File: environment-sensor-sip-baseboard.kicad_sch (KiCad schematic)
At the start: 58 parts, among them J1 USB-C_GCT_USB4105-GF-A, J2 JST_SH_1x4_SM04B-SRSS-TB-LF-SN, J3 JST_SH_1x4_SM04B-SRSS-TB-LF-SN, U1 Antmicro_GEM3, U5 SHT45, U6 BME280

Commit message: [#61553] Route PCB
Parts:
- added TP21, TP22: TP_1.5mm_SMD, antmicro-footprints:TP_SMD_1.5mm, symbol antmicroTestPoints:TP_1.5mm_SMD
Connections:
- net +3V3: now also D7.1 (C), D9.1 (C); no longer D7.2 (A), D9.2 (A)
- net GND: now also D1.2 (A), D2.2 (A), D3.2 (A), D4.2 (A), D7.2 (A), D9.2 (A), U1.A1, U1.A2, U1.A3, U1.A4, U1.A5, U1.A6, U1.B1, U1.C1, TP21.1, TP22.1; no longer D1.1 (C), D2.1 (C), D3.1 (C), D4.1 (C), D7.1 (C), D9.1 (C)
- net LD2: now also LD2.2 (A); no longer LD2.1 (C)
- net USB_CC1: now also D3.1 (C); no longer D3.2 (A)
- net USB_CC2: now also D4.1 (C); no longer D4.2 (A)
- net VBUS: now also D1.1 (C), D2.1 (C), LD1.2 (A); no longer D1.2 (A), D2.2 (A), LD1.1 (C)
- net at R5.2: now also LD2.1 (C); no longer LD2.2 (A)
- net at R12.2: now also LD1.1 (C); no longer LD1.2 (A)
- no-connect marks 22 -> 14
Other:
- moved on the sheet: D1, D2, D3, D4, D7, D9, LD1, LD2

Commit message: [#61553] Improve schematic readability
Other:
- note added: "Mechanical"
- note added: "Misc"
- note added: "SiP"
- note added: "Test Points"
- title: Environmental Sensor -> SiP Baseboard
- moved on the sheet: BAT1, C13, C2, C25, C26, C27, C28, C4, D1, D2, D3, D4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

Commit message: [#61553] Update title block
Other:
- company: Antmicro Ltd -> Antmicro 
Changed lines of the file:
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@@
     (date "2024-06-28")
     (rev "1.0.0")
-    (company "Antmicro Ltd")
+    (company "Antmicro ")
     (comment 1 "www.antmicro.com")
   )

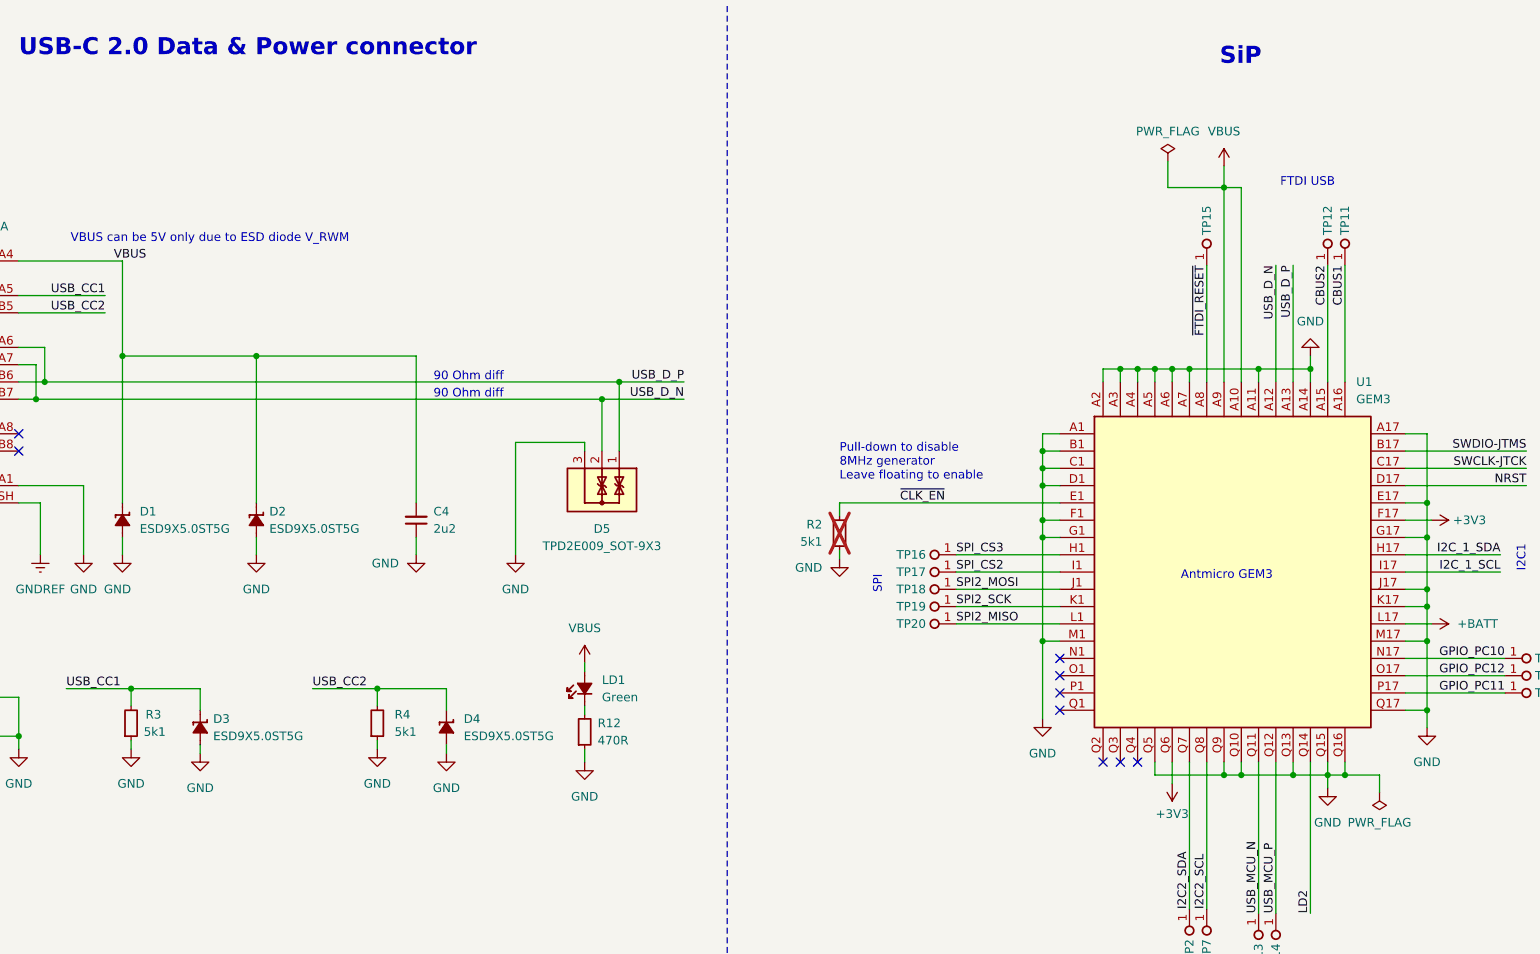
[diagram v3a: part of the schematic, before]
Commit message: [#61553] Fix ERC
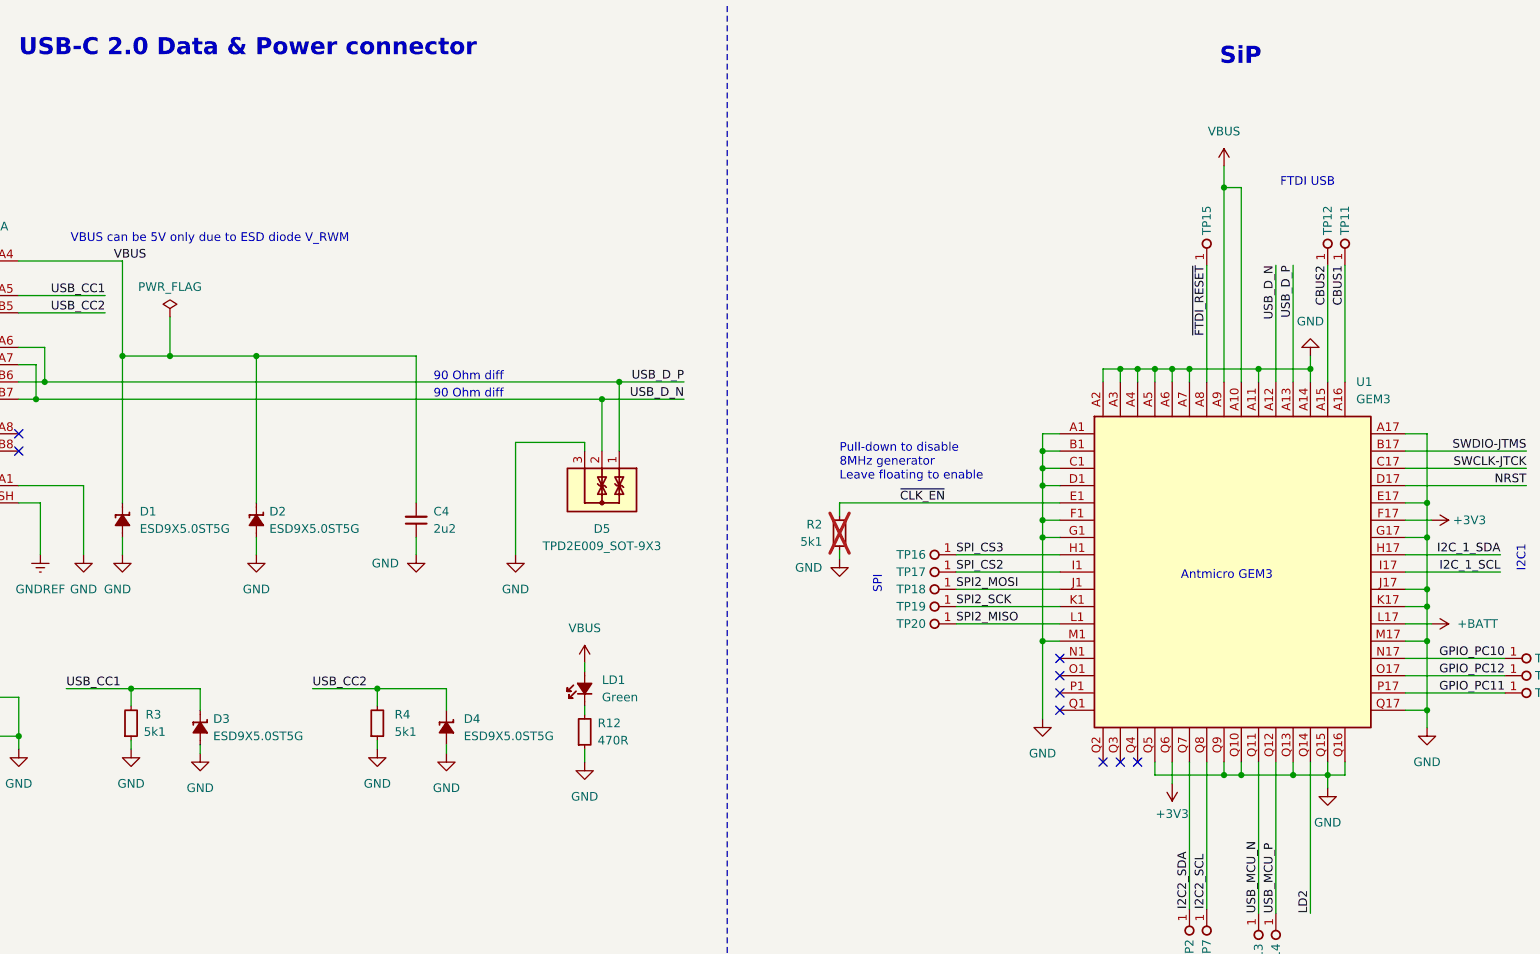
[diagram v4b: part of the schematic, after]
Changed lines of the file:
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@@
   (junction (at 49.53 67.945) (diameter 0) (color 0 0 0 0)
   )
-  (junction (at 240.665 125.73) (diameter 0) (color 0 0 0 0)
-  )
   (junction (at 238.125 125.73) (diameter 0) (color 0 0 0 0)
   )
@@
   )
   (junction (at 252.73 116.205) (diameter 0) (color 0 0 0 0)
+  )
+  (junction (at 67.945 64.135) (diameter 0) (color 0 0 0 0)
   )
   (junction (at 131.445 70.485) (diameter 0) (color 0 0 0 0)
@@
     (stroke (width 0) (type default))
   )
-  (wire (pts (xy 214.63 39.37) (xy 214.63 35.56))
+  (wire (pts (xy 67.945 58.42) (xy 67.945 64.135))
     (stroke (width 0) (type default))
   )
@@
   )
   (wire (pts (xy 205.105 66.04) (xy 205.105 67.945))
+    (stroke (width 0) (type default))
+  )
+  (wire (pts (xy 67.945 64.135) (xy 80.645 64.135))
     (stroke (width 0) (type default))
   )
@@
     (stroke (width 0) (type default))
   )
-  (wire (pts (xy 222.885 39.37) (xy 214.63 39.37))
-    (stroke (width 0) (type default))
-  )
-  (wire (pts (xy 240.665 125.73) (xy 245.745 125.73))
-    (stroke (width 0) (type default))
-  )
   (wire (pts (xy 49.53 67.945) (xy 133.985 67.945))
     (stroke (width 0) (type default))
@@
     (stroke (width 0) (type default))
   )
-  (wire (pts (xy 245.745 125.73) (xy 245.745 128.27))
-    (stroke (width 0) (type default))
-  )
   (wire (pts (xy 198.12 219.075) (xy 198.12 211.455))
     (stroke (width 0) (type default))
@@
     (stroke (width 0) (type default))
   )
-  (wire (pts (xy 60.96 64.135) (xy 80.645 64.135))
+  (wire (pts (xy 60.96 64.135) (xy 67.945 64.135))
     (stroke (width 0) (type default))
   )
@@
     )
   )
-  (symbol (lib_id "antmicropower:PWR_FLAG") (at 214.63 35.56 0) (unit 1)
-    (in_bom yes) (on_board yes) (dnp no) (fields_autoplaced)
-    (property "Reference" "#FLG01" (at 214.63 33.655 0)
-      (effects (font (size 1.27 1.27)) hide)
-    )
-    (property "Value" "PWR_FLAG" (at 214.63 31.115 0)
+  (symbol (lib_id "antmicropower:PWR_FLAG") (at 67.945 58.42 0) (unit 1)
+    (in_bom yes) (on_board yes) (dnp no) (fields_autoplaced)
+    (property "Reference" "#FLG01" (at 67.945 56.515 0)
+      (effects (font (size 1.27 1.27)) hide)
+    )
+    (property "Value" "PWR_FLAG" (at 67.945 53.975 0)
       (effects (font (size 1.27 1.27)))
     )
-    (property "Footprint" "" (at 214.63 35.56 0)
-      (effects (font (size 1.27 1.27)) hide)
-    )
-    (property "Datasheet" "" (at 214.63 35.56 0)
+    (property "Footprint" "" (at 67.945 58.42 0)
+      (effects (font (size 1.27 1.27)) hide)
+    )
+    (property "Datasheet" "" (at 67.945 58.42 0)
       (effects (font (size 1.27 1.27)) hide)
     )
@@
         )
       )
-    )
-  )
-  (symbol (lib_id "antmicropower:PWR_FLAG") (at 245.745 128.27 180) (unit 1)
-    (in_bom yes) (on_board yes) (dnp no) (fields_autoplaced)
-    (property "Reference" "#FLG02" (at 245.745 130.175 0)
-      (effects (font (size 1.27 1.27)) hide)
-    )
-    (property "Value" "PWR_FLAG" (at 245.745 132.715 0)
-      (effects (font (size 1.27 1.27)))
-    )
-    (property "Footprint" "" (at 245.745 128.27 0)
-      (effects (font (size 1.27 1.27)) hide)
-    )
-    (property "Datasheet" "" (at 245.745 128.27 0)
-      (effects (font (size 1.27 1.27)) hide)
-    )
-    (pin "1")
-    (instances
-      (project "environment-sensor-sip-baseboard"
-        (path "/8eef0f5e-ea92-4309-8bfa-5d89a1db9ae8"
-          (reference "#FLG02") (unit 1)
-        )
-      )

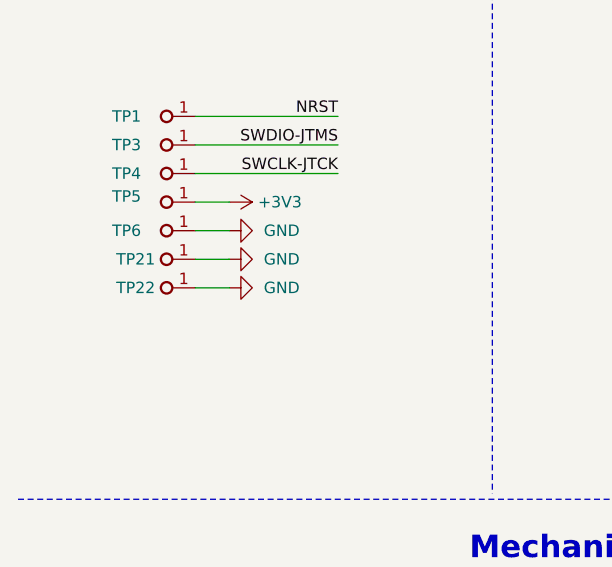
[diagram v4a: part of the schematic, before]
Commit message: [#61553] Fix logo at PCB
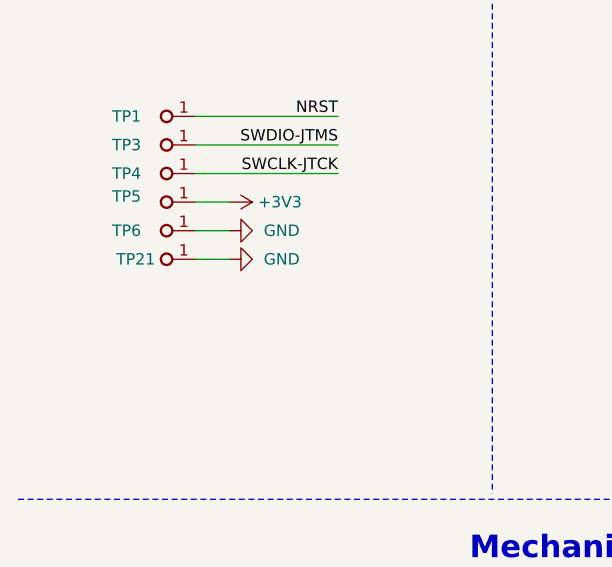
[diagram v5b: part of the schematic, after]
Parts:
- removed TP22: TP_1.5mm_SMD, antmicro-footprints:TP_SMD_1.5mm, symbol antmicroTestPoints:TP_1.5mm_SMD
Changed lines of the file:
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@@
     (stroke (width 0) (type dash))
-  )
-  (wire (pts (xy 36.83 234.315) (xy 33.02 234.315))
-    (stroke (width 0) (type default))
   )
   (wire (pts (xy 218.44 226.695) (xy 218.44 227.965))
@@
         (path "/8eef0f5e-ea92-4309-8bfa-5d89a1db9ae8"
           (reference "#PWR072") (unit 1)
-        )
-      )
-    )
-  )
-  (symbol (lib_id "antmicroTestPoints:TP_1.5mm_SMD") (at 33.02 234.315 180) (unit 1)
-    (in_bom yes) (on_board yes) (dnp no)
-    (property "Reference" "TP22" (at 28.575 234.315 0)
-      (effects (font (size 1.27 1.27) (thickness 0.15)) (justify left))
-    )
-    (property "Value" "TP_1.5mm_SMD" (at 17.78 226.695 0)
-      (effects (font (size 1.27 1.27) (thickness 0.15)) (justify left bottom) hide)
-    )
-    (property "Footprint" "antmicro-footprints:TP_SMD_1.5mm" (at 17.78 224.155 0)
-      (effects (font (size 1.27 1.27) (thickness 0.15)) (justify left bottom) hide)
-    )
-    (property "Datasheet" "" (at 17.78 221.615 0)
-      (effects (font (size 1.27 1.27) (thickness 0.15)) (justify left bottom) hide)
-    )
-    (property "MPN" "" (at 33.02 234.315 0)
-      (effects (font (size 1.27 1.27)) hide)
-    )
-    (property "Manufacturer" "" (at 33.02 234.315 0)
-      (effects (font (size 1.27 1.27)) hide)
-    )
-    (property "Author" "Antmicro" (at 17.78 219.075 0)
-      (effects (font (size 1.27 1.27) (thickness 0.15)) (justify left bottom) hide)
-    )
-    (property "License" "Apache-2.0" (at 17.78 216.535 0)
-      (effects (font (size 1.27 1.27) (thickness 0.15)) (justify left bottom) hide)
-    )
-    (property "Public" "False" (at 17.78 213.995 0)
-      (effects (font (size 1.27 1.27)) (justify left bottom) hide)
-    )
-    (pin "1")
-    (instances
-      (project "environment-sensor-sip-baseboard"
-        (path "/8eef0f5e-ea92-4309-8bfa-5d89a1db9ae8"
-          (reference "TP22") (unit 1)
         )
       )
@@
         )
       )
-    )
-  )
-  (symbol (lib_id "antmicropower:GND") (at 36.83 234.315 90) (mirror x) (unit 1)
-    (in_bom yes) (on_board yes) (dnp no) (fields_autoplaced)
-    (property "Reference" "#PWR028" (at 43.18 234.315 0)
-      (effects (font (size 1.27 1.27)) hide)
-    )
-    (property "Value" "GND" (at 40.64 234.315 90)
-      (effects (font (size 1.27 1.27)) (justify right))
-    )
-    (property "Footprint" "" (at 36.83 234.315 0)
-      (effects (font (size 1.27 1.27)) hide)
-    )
-    (property "Datasheet" "" (at 36.83 234.315 0)
-      (effects (font (size 1.27 1.27)) hide)
-    )
-    (property "Author" "Antmicro" (at 44.45 243.205 0)
-      (effects (font (size 1.27 1.27) (thickness 0.15)) (justify left bottom) hide)
-    )
-    (property "License" "Apache-2.0" (at 46.99 243.205 0)
-      (effects (font (size 1.27 1.27) (thickness 0.15)) (justify left bottom) hide)
-    )
-    (pin "1")
-    (instances
-      (project "environment-sensor-sip-baseboard"
-        (path "/8eef0f5e-ea92-4309-8bfa-5d89a1db9ae8"
-          (reference "#PWR028") (unit 1)
-        )
-      )

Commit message: [#62396] Update components
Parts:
- U1: value Antmicro_GEM3 -> Myra-231F1F08; footprint antmicro-footprints:LGA-64_11.4x11.4mm_GEM3-footprint -> antmicro-footprints:LGA-64_11.4x11.4mm_Myra; symbol antmicroModules:GEM3 -> antmicroModules:Myra-231F1F08; MPN GEM3 -> Myra-231F1F08
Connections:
- net GND: no longer U1.B1, U1.C1
- no-connect marks 14 -> 7
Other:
- note removed: "Antmicro GEM3"
- note removed: "FTDI USB"
- note removed: "I2C1"
- note removed: "I2C2"
- note removed: "SPI"
- note removed: "STM USB"
- moved on the sheet: R2, TP10, TP11, TP12, TP13, TP14, TP15, TP16, TP17, TP18, TP19, TP2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
